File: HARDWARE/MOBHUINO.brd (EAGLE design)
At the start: 93.2 x 61.9 mm, 28 parts, among them IC1 7805T, IC2 MEGA328-P, Q1 16 MHz, U1 ARDUINO_SHIELDNO_SILK, X2 USB

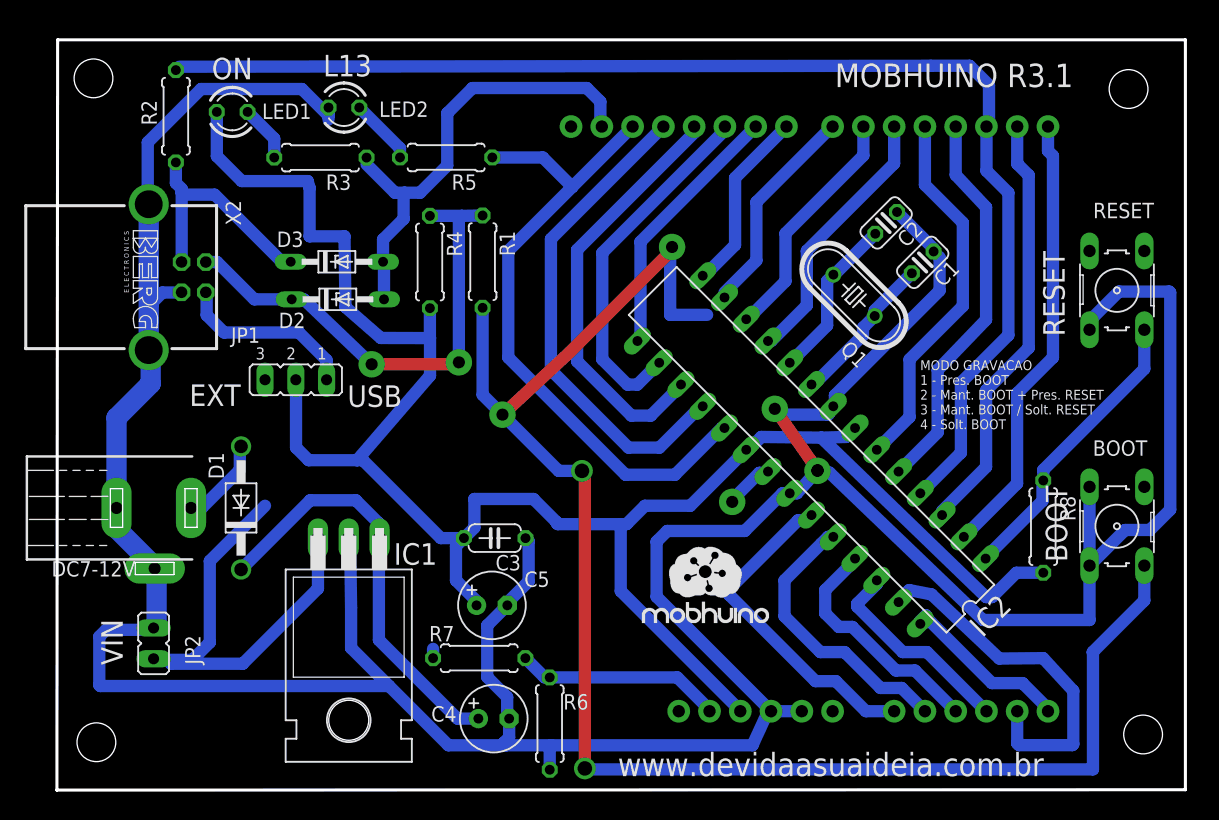
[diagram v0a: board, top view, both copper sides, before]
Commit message: - Inserção da malha de terra - Melhorado algumas trilhas - Modificado a linha de corte externa mais para mais grossa
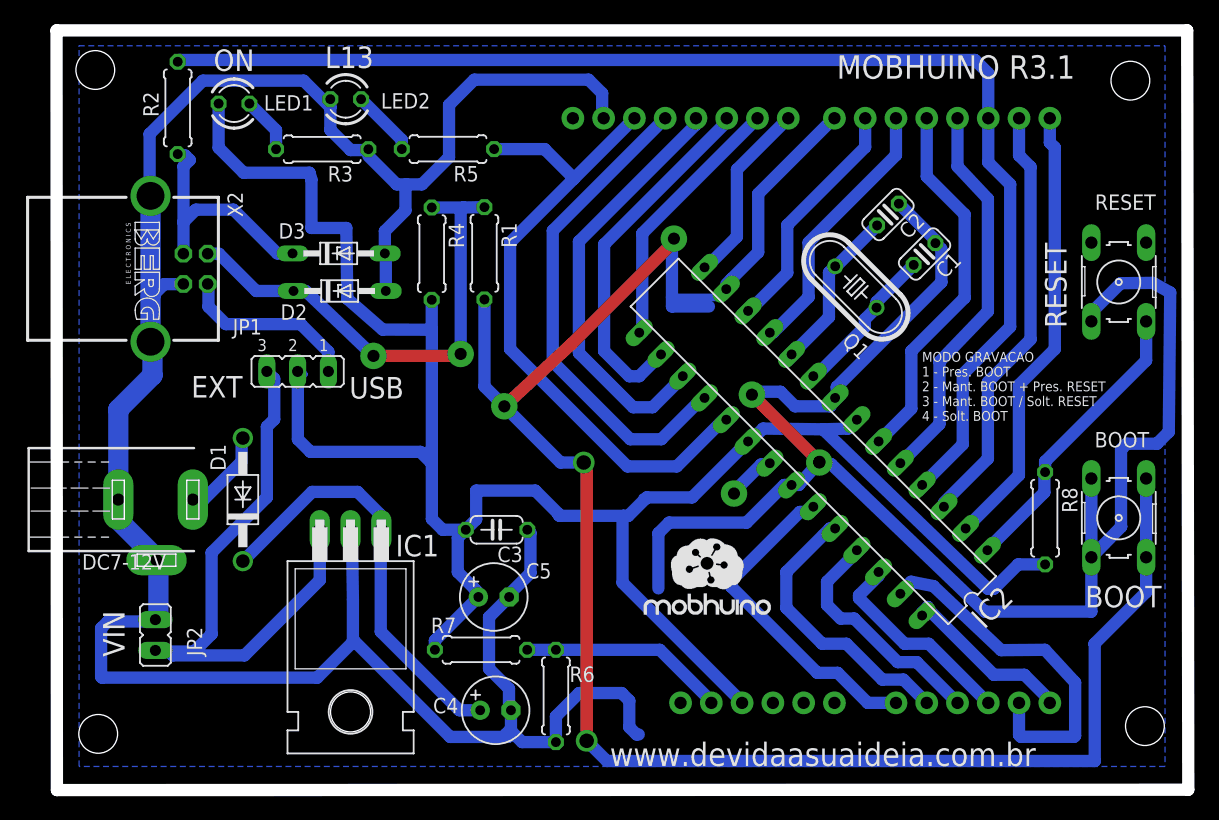
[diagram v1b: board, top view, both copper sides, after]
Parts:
- moved R6 2.34 mm to (41.1, 7.74)
- moved D2 0.71 mm to (23.3, 41.2)
- moved D3 0.71 mm to (23.2, 44.3)
- moved R5 0.71 mm to (32.2, 52.9)
- moved BOOT 0.71 mm to (87.6, 22.4)
- moved IC2 0.71 mm to (62.4, 28.8)
- moved R7 0.71 mm to (35.0, 11.6)
- moved R8 0.71 mm to (81.5, 22.4)
- moved C3 0.71 mm to (36.2, 21.5)
- moved JP2 0.71 mm to (8.07, 12.8)
- moved C4 0.71 mm to (36.1, 6.56)
- moved C5 0.71 mm to (36.0, 15.9)
- moved IC1 0.71 mm to (24.2, 11.2)
- moved C1 0.71 mm to (71.6, 44.2)
- moved C2 0.71 mm to (68.5, 47.5)
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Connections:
- removed net N$24: IC1.3, JP2.1
- net EXT_+5V: now also IC1.3, JP2.1
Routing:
- net EXT_+5V: track 0.00 -> 48.6 mm
- net N$24: track 37.7 -> 0.00 mm
- net GND: track 350.4 -> 332.5 mm
- net D7: track 149.1 -> 161.3 mm
- net +5V: track 160.8 -> 170.5 mm
- net D2: track 105.9 -> 105.2 mm
- added copper zone on layer 16, net GND
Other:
- board size 93.2 x 61.9 mm -> 93.4 x 62.7 mm

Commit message: - Atualizado logo do Mobhuino
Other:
- outline, holes or cut-outs redrawn
